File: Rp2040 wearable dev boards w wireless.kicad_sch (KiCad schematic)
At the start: 80 parts, among them IC1 NRF24L01P-R7, J1 battery plug, J2 UJ31-CH-31-SMT-TR, J3 Conn_01x20, J4 Conn_01x20, J5 Conn_01x04, J6 EMPCB.SMAFSTJ.B.HT, Q1 Si2301, SW1 B3U-1100P, SW2 power Switch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

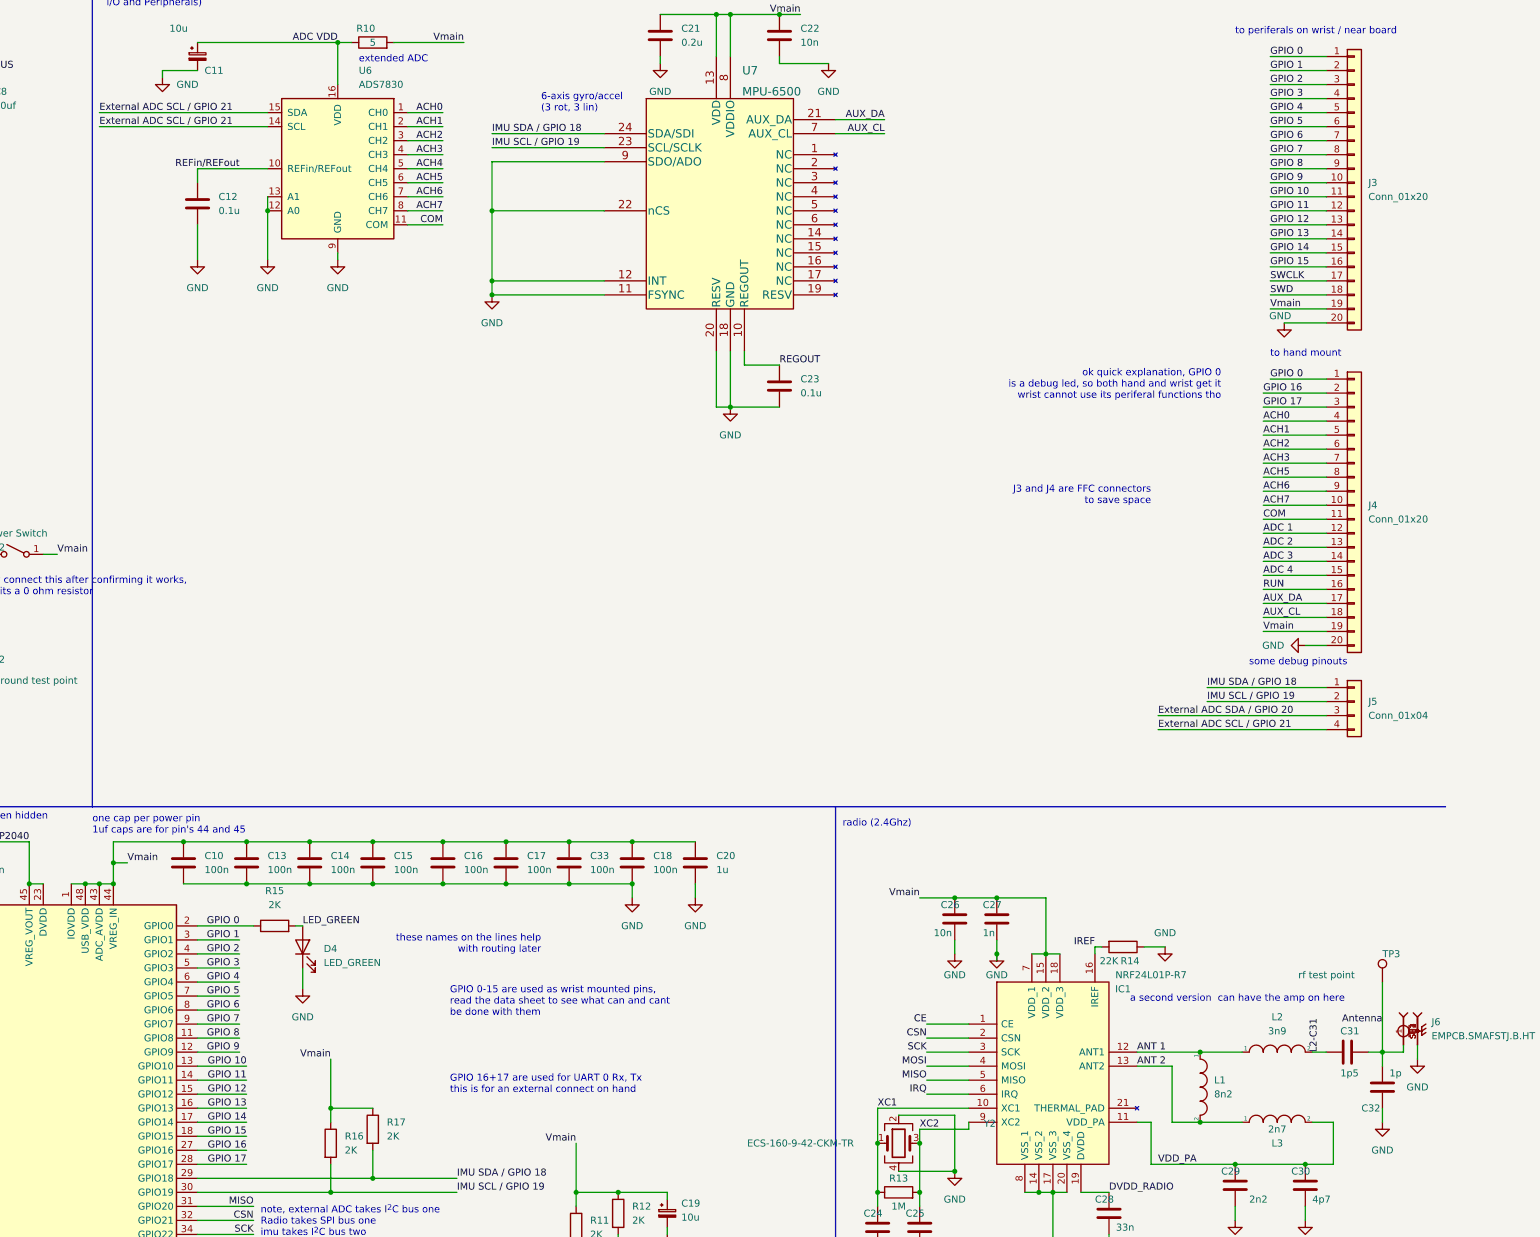
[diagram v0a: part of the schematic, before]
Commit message: finished pcb route v1, asked the electronics discord if they could verify it.
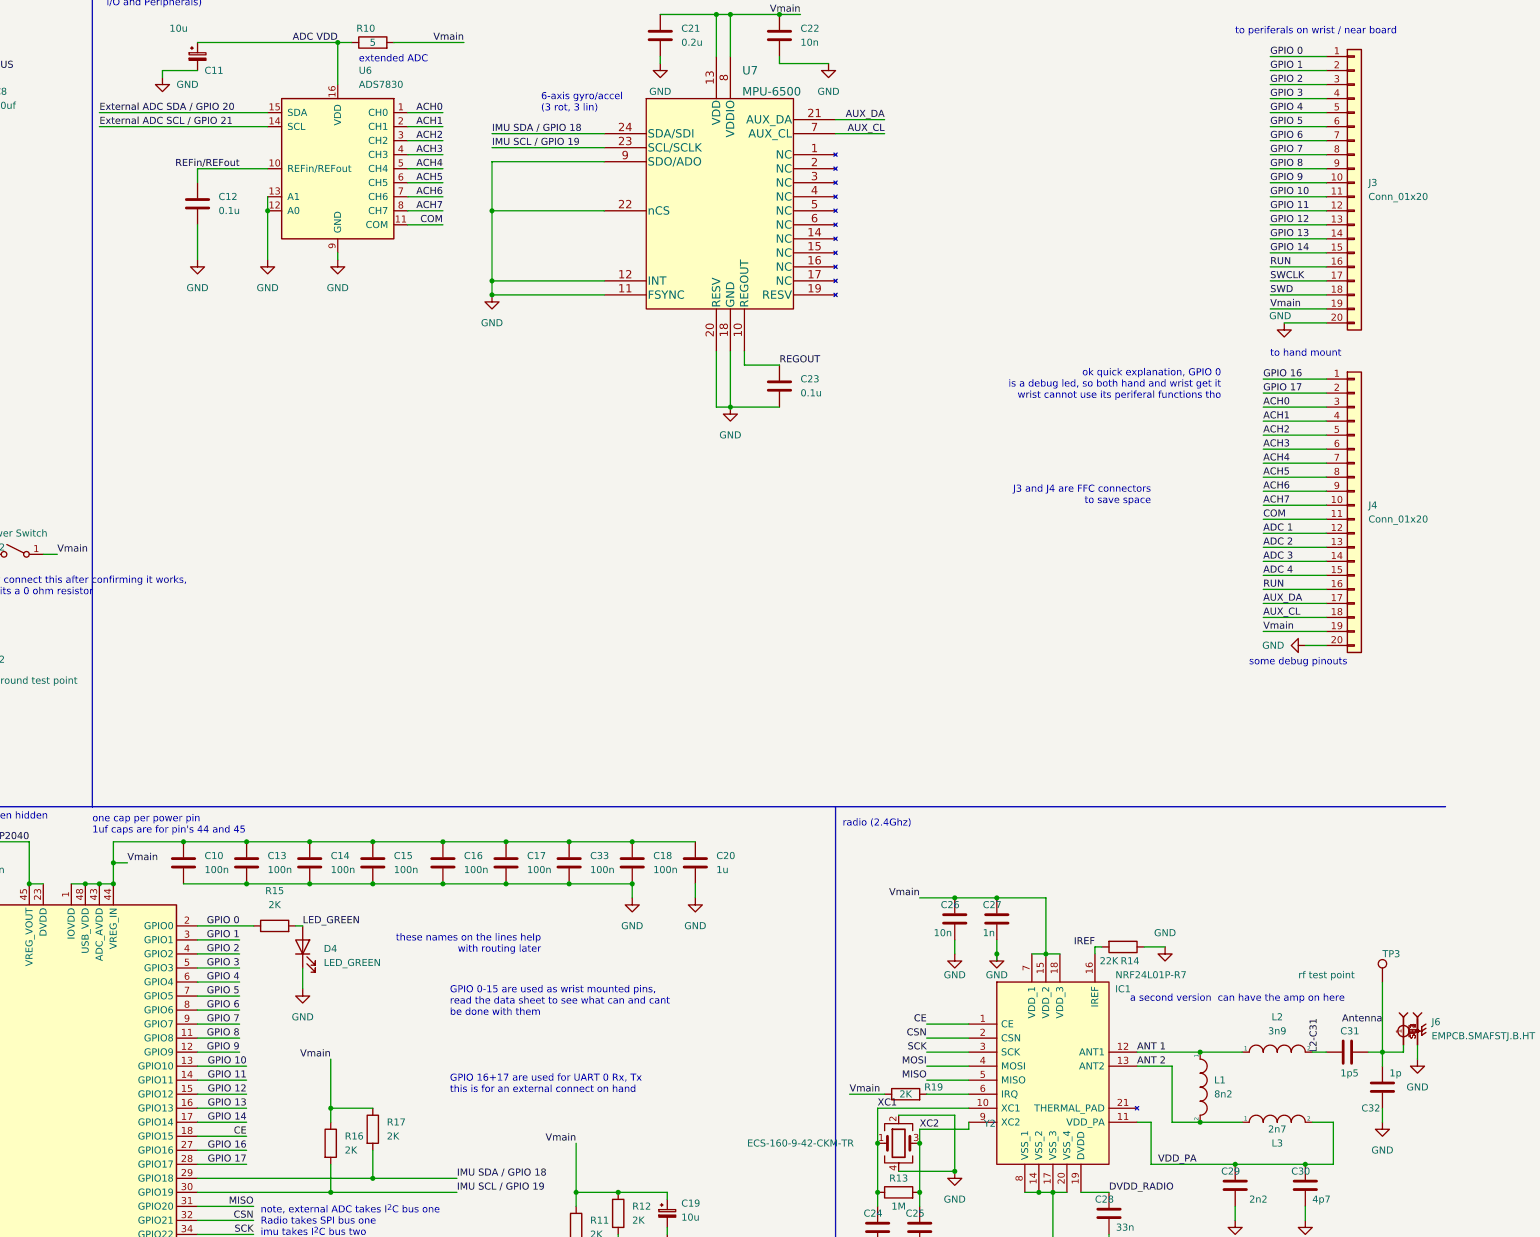
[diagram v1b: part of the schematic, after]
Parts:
- removed J5: Conn_01x04, Connector_PinSocket_2.54mm:PinSocket_2x02_P2.54mm_Horizontal, symbol Connector_Generic:Conn_01x04
- added R19: 2K, Resistor_SMD:R_0402_1005Metric, symbol Device:R
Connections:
- net ACH0: now also J4.3 (Pin_3); no longer J4.4 (Pin_4)
- net ACH1: now also J4.4 (Pin_4); no longer J4.5 (Pin_5)
- net ACH2: now also J4.5 (Pin_5); no longer J4.6 (Pin_6)
- net ACH3: now also J4.6 (Pin_6); no longer J4.7 (Pin_7)
- net ACH4: now also J4.7 (Pin_7)
- net CE: now also U5.18 (GPIO15)
- net External ADC SCL / GPIO 21: no longer U6.15 (SDA)
- net External ADC SDA / GPIO 20: now also U6.15 (SDA)
- net GPIO 0: no longer J4.1 (Pin_1)
- net GPIO 16: now also J4.1 (Pin_1); no longer J4.2 (Pin_2)
- net GPIO 17: now also J4.2 (Pin_2); no longer J4.3 (Pin_3)
- net RUN: now also J3.16 (Pin_16)
- net Vmain: now also R19.1
- removed net GPIO 15: J3.16 (Pin_16), U5.18 (GPIO15)
- net IRQ: no longer names the net of IC1.6 (IRQ)
- net IRQ: now also R19.2
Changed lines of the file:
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@@
     (stroke (width 0) (type default) (color 0 0 0 0))
   )
-  (wire (pts (xy 367.03 140.97) (xy 388.62 140.97))
-    (stroke (width 0) (type default) (color 0 0 0 0))
-  )
   (wire (pts (xy 184.15 209.55) (xy 193.04 209.55))
     (stroke (width 0) (type default) (color 0 0 0 0))
@@
     (stroke (width 0) (type default) (color 0 0 0 0))
   )
-  (wire (pts (xy 358.14 146.05) (xy 388.62 146.05))
-    (stroke (width 0) (type default) (color 0 0 0 0))
-  )
   (wire (pts (xy 184.15 224.79) (xy 193.04 224.79))
     (stroke (width 0) (type default) (color 0 0 0 0))
@@
     (stroke (width 0) (type default) (color 0 0 0 0))
   )
-  (wire (pts (xy 378.46 82.55) (xy 388.62 82.55))
+  (wire (pts (xy 377.19 82.55) (xy 388.62 82.55))
     (stroke (width 0) (type default) (color 0 0 0 0))
   )
@@
     (stroke (width 0) (type default) (color 0 0 0 0))
   )
+  (wire (pts (xy 302.26 212.09) (xy 308.61 212.09))
+    (stroke (width 0) (type default) (color 0 0 0 0))
+  )
   (wire (pts (xy 62.23 35.56) (xy 82.55 35.56))
     (stroke (width 0) (type default) (color 0 0 0 0))
@@
     (stroke (width 0) (type default) (color 0 0 0 0))
   )
-  (wire (pts (xy 358.14 143.51) (xy 388.62 143.51))
-    (stroke (width 0) (type default) (color 0 0 0 0))
-  )
   (wire (pts (xy 166.37 173.99) (xy 168.91 173.99))
     (stroke (width 0) (type default) (color 0 0 0 0))
@@
     (stroke (width 0) (type default) (color 0 0 0 0))
   )
-  (wire (pts (xy 367.03 138.43) (xy 388.62 138.43))
-    (stroke (width 0) (type default) (color 0 0 0 0))
-  )
   (wire (pts (xy 82.55 40.64) (xy 93.98 40.64))
     (stroke (width 0) (type default) (color 0 0 0 0))
@@
     (effects (font (size 1.27 1.27)) (justify left bottom))
   )
-  (label "IRQ" (at 316.23 212.09 180)
-    (effects (font (size 1.27 1.27)) (justify right bottom))
-  )
   (label "USB+" (at 101.6 185.42 0)
     (effects (font (size 1.27 1.27)) (justify left bottom))
@@
     (effects (font (size 1.27 1.27)) (justify right bottom))
   )
-  (label "ACH0" (at 377.19 90.17 0)
-    (effects (font (size 1.27 1.27)) (justify left bottom))
-  )
-  (label "IMU SDA {slash} GPIO 18" (at 367.03 138.43 0)
+  (label "ACH0" (at 377.19 87.63 0)
     (effects (font (size 1.27 1.27)) (justify left bottom))
   )
@@
     (effects (font (size 1.27 1.27)) (justify left bottom))
   )
-  (label "External ADC SCL {slash} GPIO 21" (at 358.14 146.05 0)
-    (effects (font (size 1.27 1.27)) (justify left bottom))
-  )
   (label "MOSI" (at 316.23 207.01 180)
     (effects (font (size 1.27 1.27)) (justify right bottom))
@@
     (effects (font (size 1.27 1.27)) (justify right bottom))
   )
-  (label "ACH3" (at 377.19 97.79 0)
+  (label "ACH3" (at 377.19 95.25 0)
     (effects (font (size 1.27 1.27)) (justify left bottom))
   )
@@
     (effects (font (size 1.27 1.27)) (justify left bottom))
   )
-  (label "ACH1" (at 377.19 92.71 0)
+  (label "ACH1" (at 377.19 90.17 0)
     (effects (font (size 1.27 1.27)) (justify left bottom))
   )
@@
     (effects (font (size 1.27 1.27)) (justify right bottom))
   )
-  (label "GPIO 0" (at 378.46 82.55 0)
-    (effects (font (size 1.27 1.27)) (justify left bottom))
-  )
   (label "RUN" (at 377.19 120.65 0)
     (effects (font (size 1.27 1.27)) (justify left bottom))
@@
     (effects (font (size 1.27 1.27)) (justify right bottom))
   )
-  (label "GPIO 17" (at 377.19 87.63 0)
+  (label "GPIO 17" (at 377.19 85.09 0)
     (effects (font (size 1.27 1.27)) (justify left bottom))
   )
@@
     (effects (font (size 1.27 1.27)) (justify left bottom))
   )
-  (label "External ADC SDA {slash} GPIO 20" (at 358.14 143.51 0)
-    (effects (font (size 1.27 1.27)) (justify left bottom))
-  )
   (label "GPIO 16" (at 193.04 222.25 180)
     (effects (font (size 1.27 1.27)) (justify right bottom))
@@
     (effects (font (size 1.27 1.27)) (justify right bottom))
   )
+  (label "RUN" (at 378.46 62.23 0)
+    (effects (font (size 1.27 1.27)) (justify left bottom))
+  )
   (label "GPIO 12" (at 378.46 54.61 0)
     (effects (font (size 1.27 1.27)) (justify left bottom))
@@
     (effects (font (size 1.27 1.27)) (justify right bottom))
   )
-  (label "External ADC SCL {slash} GPIO 21" (at 166.37 34.29 0)
+  (label "External ADC SDA {slash} GPIO 20" (at 166.37 34.29 0)
     (effects (font (size 1.27 1.27)) (justify left bottom))
   )
@@
     (effects (font (size 1.27 1.27)) (justify right bottom))
   )
+  (label "ACH4" (at 377.19 97.79 0)
+    (effects (font (size 1.27 1.27)) (justify left bottom))
+  )
   (label "USB_R-" (at 124.46 191.77 180)
     (effects (font (size 1.27 1.27)) (justify right bottom))
   )
+  (label "Vmain" (at 302.26 212.09 0)
+    (effects (font (size 1.27 1.27)) (justify left bottom))
+  )
   (label "Antenna" (at 398.78 199.39 180)
     (effects (font (size 1.27 1.27)) (justify right bottom))
@@
     (effects (font (size 1.27 1.27)) (justify right bottom))
   )
-  (label "ACH2" (at 377.19 95.25 0)
+  (label "ACH2" (at 377.19 92.71 0)
     (effects (font (size 1.27 1.27)) (justify left bottom))
   )
@@
     (effects (font (size 1.27 1.27)) (justify right bottom))
   )
-  (label "GPIO 16" (at 377.19 85.09 0)
+  (label "GPIO 16" (at 377.19 82.55 0)
     (effects (font (size 1.27 1.27)) (justify left bottom))
   )
@@
     (effects (font (size 1.27 1.27)) (justify right bottom))
   )
-  (label "GPIO 15" (at 193.04 219.71 180)
+  (label "CE" (at 193.04 219.71 180)
     (effects (font (size 1.27 1.27)) (justify right bottom))
   )
@@
     (effects (font (size 1.27 1.27)) (justify right bottom))
   )
-  (label "GPIO 15" (at 378.46 62.23 0)
-    (effects (font (size 1.27 1.27)) (justify left bottom))
-  )
-  (label "IMU SCL {slash} GPIO 19" (at 367.03 140.97 0)
-    (effects (font (size 1.27 1.27)) (justify left bottom))
-  )
   (symbol (lib_id "Regulator_Linear:NCP1117-3.3_TO252") (at 121.92 114.3 0) (unit 1)
     (in_bom yes) (on_board yes) (fields_autoplaced)
@@
     (pin "1")
   )
+  (symbol (lib_id "Device:R") (at 312.42 212.09 90) (unit 1)
+    (in_bom yes) (on_board yes)
+    (property "Reference" "R19" (id 0) (at 317.5 210.82 90))
+    (property "Value" "2K" (id 1) (at 312.42 212.09 90))
+    (property "Footprint" "Resistor_SMD:R_0402_1005Metric" (id 2) (at 312.42 213.868 90)
+      (effects (font (size 1.27 1.27)) hide)
+    )
+    (property "Datasheet" "~" (id 3) (at 312.42 212.09 0)
+      (effects (font (size 1.27 1.27)) hide)
+    )
+    (pin "1")
+    (pin "2")
+  )
   (symbol (lib_id "Device:C") (at 215.9 170.18 0) (unit 1)
     (in_bom yes) (on_board yes) (fields_autoplaced)
@@
     (pin "1")
   )
-  (symbol (lib_id "Connector_Generic:Conn_01x04") (at 393.7 140.97 0) (unit 1)
-    (in_bom yes) (on_board yes) (fields_autoplaced)
-    (property "Reference" "J5" (id 0) (at 396.24 140.9699 0)
-      (effects (font (size 1.27 1.27)) (justify left))
-    )
-    (property "Value" "Conn_01x04" (id 1) (at 396.24 143.5099 0)
-      (effects (font (size 1.27 1.27)) (justify left))
-    )
-    (property "Footprint" "Connector_PinSocket_2.54mm:PinSocket_2x02_P2.54mm_Horizontal" (id 2) (at 393.7 140.97 0)
-      (effects (font (size 1.27 1.27)) hide)
-    )
-    (property "Datasheet" "~" (id 3) (at 393.7 140.97 0)
-      (effects (font (size 1.27 1.27)) hide)
-    )
-    (pin "1")
-    (pin "2")
-    (pin "3")
-    (pin "4")
-  )
   (symbol (lib_id "Device:R") (at 69.85 113.03 0) (unit 1)
     (in_bom yes) (on_board yes) (fields_autoplaced)
@@
       (reference "J4") (unit 1) (value "Conn_01x20") (footprint "Connector_FFC-FPC:TE_2-84952-0_1x20-1MP_P1.0mm_Horizontal")
     )
-    (path "/6a09e7a1-f919-4ff2-98d6-23587c158b4f"
-      (reference "J5") (unit 1) (value "Conn_01x04") (footprint "Connector_PinSocket_2.54mm:PinSocket_2x02_P2.54mm_Horizontal")
-    )
     (path "/b90eba54-a2c0-4abe-9681-85b3b2ee653b"
       (reference "J6") (unit 1) (value "EMPCB.SMAFSTJ.B.HT") (footprint "TAOGLAS_EMPCB.SMAFSTJ.B.HT")
@@
       (reference "R18") (unit 1) (value "0") (footprint "Resistor_SMD:R_0402_1005Metric")
     )
+    (path "/44cac171-8875-4d5d-8407-e8e65caa3547"
+      (reference "R19") (unit 1) (value "2K") (footprint "Resistor_SMD:R_0402_1005Metric")
+    )
     (path "/8b43026f-9599-44ad-9691-8c4a0d288de4"

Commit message: finished cap bom, need to reroute part of it to fit cap sizes
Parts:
- C1, C2: Digikey Part  Number (none) -> 445-7173-6-ND
- C10, C13, C14, C15, C16, C17, C18, C3, C33, C6, C7: value 100n -> 0.1u; footprint Capacitor_SMD:C_01005_0402Metric -> Capacitor_SMD:C_0201_0603Metric; Digikey Part  Number (none) -> 490-3167-1-ND
- C11, C19: Digikey Part  Number (none) -> 732-6416-6-ND
- C12, C23: footprint Capacitor_SMD:C_01005_0402Metric -> Capacitor_SMD:C_0201_0603Metric; Digikey Part  Number (none) -> 490-3167-1-ND
- C20, C4: footprint Capacitor_SMD:C_01005_0402Metric -> Capacitor_SMD:C_0201_0603Metric; Digikey Part  Number (none) -> 478-7862-1-ND
- C21: footprint Capacitor_SMD:C_01005_0402Metric -> Capacitor_SMD:C_1206_3216Metric; Digikey Part  Number (none) -> 478-12814-1-ND
- C22, C26: Digikey Part  Number (none) -> 490-13319-1-ND
- C24, C25: footprint Capacitor_SMD:C_01005_0402Metric -> Capacitor_SMD:C_0402_1005Metric; Digikey Part  Number (none) -> 490-GJM1555C1H140FB01DCT-ND
- C27: Digikey Part  Number (none) -> 490-GRM022R71C102KE14LCT-ND
- C28: Digikey Part  Number (none) -> 490-9977-1-ND
- C29: Digikey Part  Number (none) -> 490-7164-1-ND
- C30: Digikey Part  Number (none) -> 490-13585-1-ND
- C31: Digikey Part  Number (none) -> 490-13488-1-ND
- C32: Digikey Part  Number (none) -> 490-13474-1-ND
- C5, C8, C9: footprint Capacitor_SMD:C_01005_0402Metric -> Capacitor_SMD:C_0402_1005Metric; Digikey Part  Number (none) -> 490-GRM155R60J106ME05JCT-ND
- IC1: Arrow Part Number NRF24L01P-R7 -> (none); Arrow Price/Stock https://www.arrow.com/en/products/nrf24l01p-r7/nordic-semic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 -> (none); Digikey Part  Number (none) -> 1490-1033-1-ND

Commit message: more bom creation
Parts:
- removed J2: UJ31-CH-31-SMT-TR, usb-c footprint:CUI_UJ31-CH-31-SMT-TR, symbol Connector:USB_C_Receptacle
- removed TP2: ground test point, TestPoint:TestPoint_Pad_D2.0mm, symbol Connector:TestPoint
- added J2: DX07S016JA1R1500, JAE_DX07S016JA1R1500, symbol usb-c usb 2.0:DX07S016JA1R1500
- D1: Digikey Part  Number (none) -> 160-1827-1-ND
- D2: Digikey Part  Number (none) -> 641-1690-1-ND
- D3: Digikey Part  Number (none) -> 160-1448-1-ND
- D4: Digikey Part  Number (none) -> 160-1446-1-ND
- J1: Digikey Part  Number (none) -> 455-1749-1-ND
- J3, J4: Digikey Part  Number (none) -> A100319CT-ND
- J6: Digikey Part  Number (none) -> 931-1175-ND
- L1: Digikey Part  Number (none) -> 490-6849-1-ND
- L2: Digikey Part  Number (none) -> 490-6813-1-ND
- L3: Digikey Part  Number (none) -> 490-6799-1-ND
- Q1: Digikey Part  Number (none) -> 353-SI2301A-TPCT-ND
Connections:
- net CC1: now also J2.3 (CC1)
- net CC2: now also J2.9 (CC2)
- net GND: now also J2.1 (GND), J2.12 (GND), J2.S1 (SHIELD), J2.S2 (SHIELD), J2.S3 (SHIELD), J2.S4 (SHIELD), J2.S5 (SHIELD), J2.S6 (SHIELD)
- net USB+: now also U3.4 (D2+), U3.7 (NC), J2.6 (D+), J2.7 (D+); no longer U3.5 (D2-), U3.6 (NC)
- net USB-: now also U3.5 (D2-), U3.6 (NC), J2.5 (D-), J2.8 (D-); no longer U3.4 (D2+), U3.7 (NC)
- net VBUS: now also J2.11 (VBUS), J2.2 (VBUS)
- no-connect marks 10 -> 0
